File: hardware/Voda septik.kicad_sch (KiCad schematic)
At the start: 41 parts, among them J1 Napájení a 4-20mA senzory, J2 Screw_Terminal_01x09, J3 Display LCD I2C, J4 Display TM1637, U1 DC-DC 24V -> 5V, U2 MAX3485-modul, U3 ADS1115IDGS, U4 ESP32-DevKitC, U5 CA56-12CGKWA

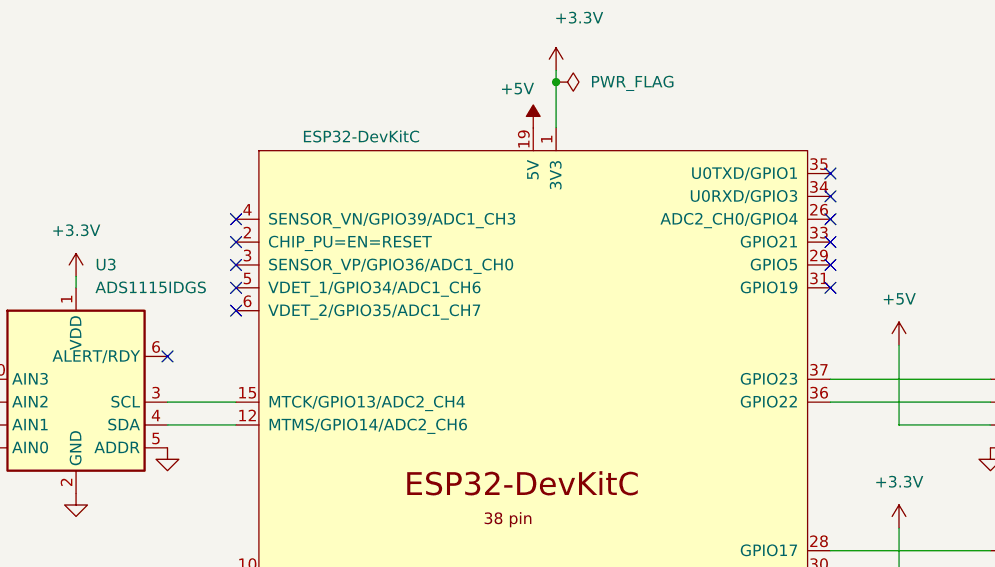
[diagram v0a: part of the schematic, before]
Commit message: Dokreslit propojku RDY/ALERT
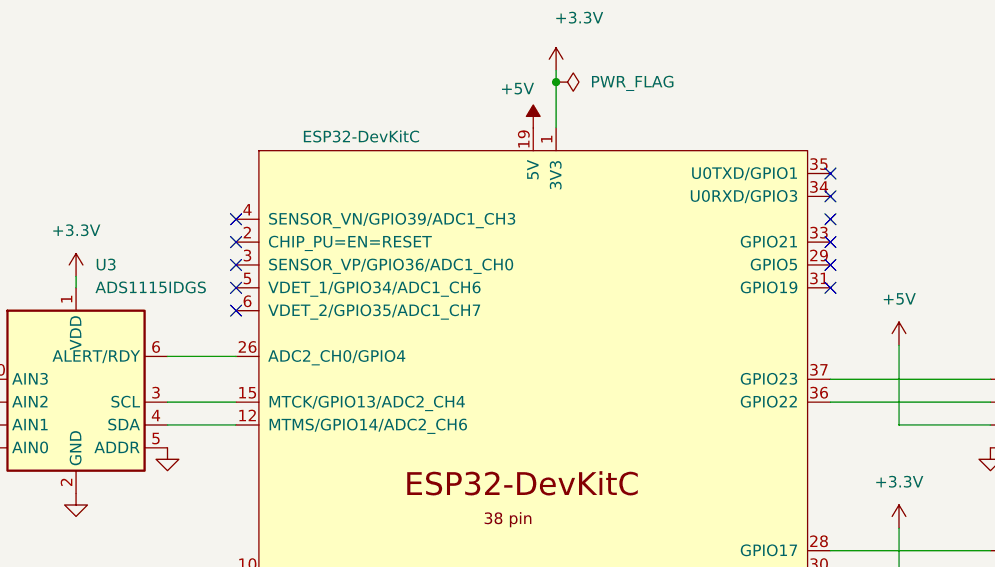
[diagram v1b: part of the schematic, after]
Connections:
- net at U4.26 (ADC2_CH0/GPIO4): now also U3.6 (ALERT/RDY)
- no-connect marks 14 -> 13
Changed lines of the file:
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@@
-	)
-	(no_connect
-		(at 179.07 50.8)
 	)
 	(no_connect
@@
 		)
 		(stroke
+			(width 0)
+			(type default)
+		)
+	)
+	(wire
+		(pts
+			(xy 179.07 50.8) (xy 186.69 50.8)
+		)
+		(stroke
